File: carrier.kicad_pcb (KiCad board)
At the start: 4 copper layers, 20.3 x 68.6 mm, 41 parts, among them J1 Conn_02x06_Odd_Even, J10 Conn_01x02, J2 Conn_01x26, J3 Conn_01x26, J4 TYPE-C-31-M-12, J5 Conn_01x02, J6 Conn_01x02, J7 Conn_01x02, J8 Conn_01x02, J9 Conn_01x02, U1 CARAVEL, U2 W25Q128JVS, U3 LP5907MFX-3.3, U4 LP5907MFX-1.8, U5 LP5907MFX-1.8, U6 LP5907MFX-3.3, U7 TPD2E001DRSR, X1 SG-5032CAN

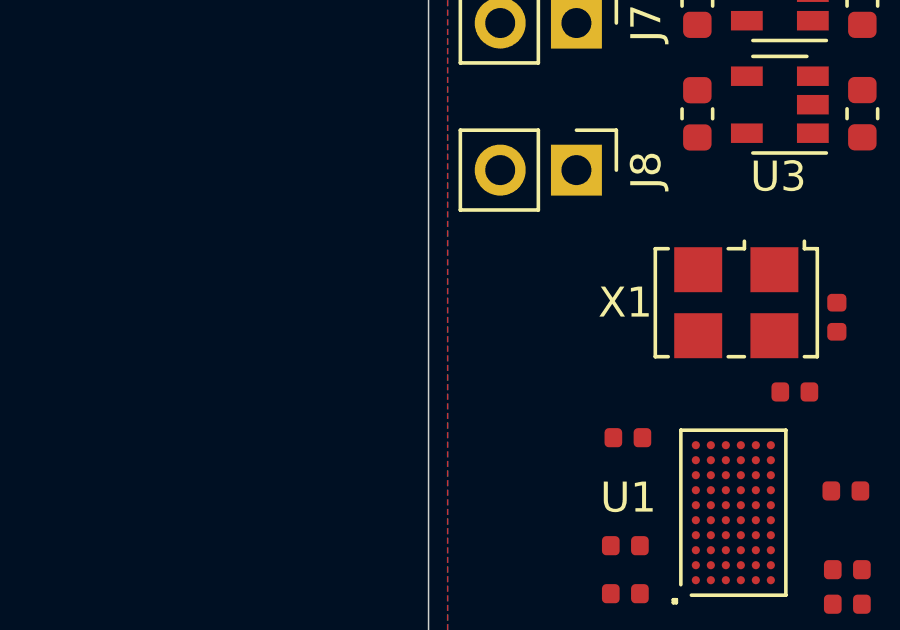
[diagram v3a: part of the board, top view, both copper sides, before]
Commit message: Add provision for external clk on  pin header
Uses a solder jumper to select oscillator by default.
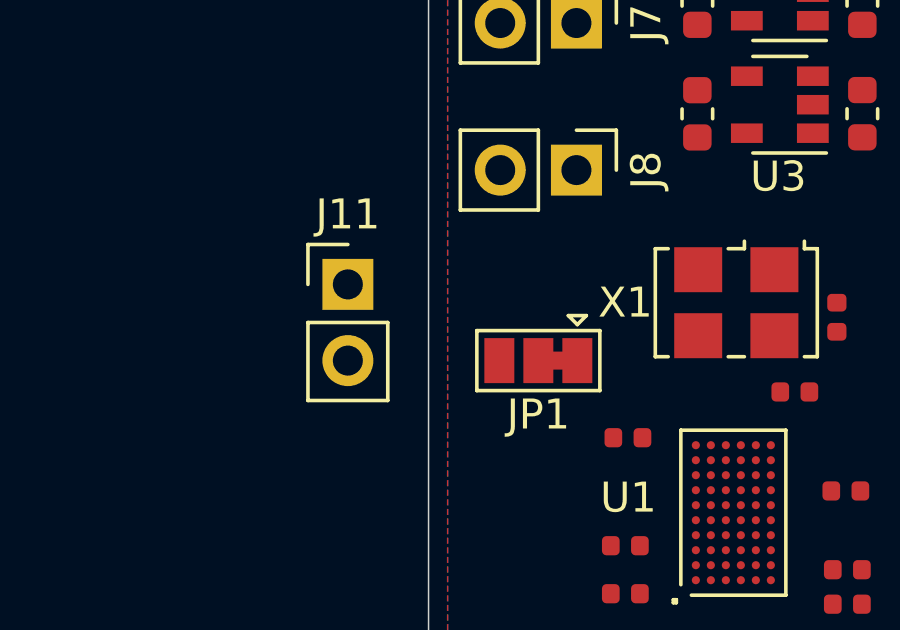
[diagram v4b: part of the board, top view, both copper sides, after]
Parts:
- added J11: Conn_01x02, Connector_PinHeader_2.54mm:PinHeader_1x02_P2.54mm_Vertical, F.Cu at (55.9, 72.4)
- added JP1: SolderJumper_3_Bridged12, Jumper:SolderJumper-3_P1.3mm_Bridged12_Pad1.0x1.5mm, F.Cu at (62.2, 74.9)
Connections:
- X1 pad 3: clock -> Net-(X1-Pad3)
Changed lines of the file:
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@@
   (net 78 "Net-(J4-PadA4B9)")
   (net 79 "unconnected-(J2-Pad3)")
+  (net 80 "Net-(X1-Pad3)")
+  (net 81 "Net-(J11-Pad1)")
   (footprint "Connector_PinHeader_2.54mm:PinHeader_1x26_P2.54mm_Vertical" (layer "F.Cu")
     (at 41.0972 46.6344)
@@
       (net 3 "GND") (pinfunction "GND") (pintype "power_in"))
     (pad "3" smd rect locked (at 1.27 -1.1 180) (size 1.6 1.5) (layers "F.Cu" "F.Paste" "F.Mask")
-      (net 22 "clock") (pinfunction "OUT") (pintype "output"))
+      (net 80 "Net-(X1-Pad3)") (pinfunction "OUT") (pintype "output"))
     (pad "4" smd rect locked (at -1.27 -1.1 180) (size 1.6 1.5) (layers "F.Cu" "F.Paste" "F.Mask")
       (net 7 "vdda") (pinfunction "VCC") (pintype "power_in"))
@@
     )
   )
+  (footprint "Jumper:SolderJumper-3_P1.3mm_Bridged12_Pad1.0x1.5mm" (layer "F.Cu")
+    (at 62.23 74.93 180)
+    (descr "SMD Solder 3-pad Jumper, 1x1.5mm Pads, 0.3mm gap, pads 1-2 bridged with 1 copper strip")
+    (tags "solder jumper open")
+    (property "Sheetfile" "carrier.kicad_sch")
+    (property "Sheetname" "")
+    (attr exclude_from_pos_files)
+    (fp_text reference "JP1" (at 0 -1.8) (layer "F.SilkS")
+      (effects (font (size 1 1) (thickness 0.15)))
+    )
+    (fp_text value "SolderJumper_3_Bridged12" (at 0 2) (layer "F.Fab")
+      (effects (font (size 1 1) (thickness 0.15)))
+    )
+    (fp_poly (pts
+        (xy -0.9 -0.3)
+        (xy -0.4 -0.3)
+        (xy -0.4 0.3)
+        (xy -0.9 0.3)
+      ) (layer "F.Cu") (width 0) (fill solid))
+    (fp_line (start 2.05 -1) (end 2.05 1) (layer "F.SilkS") (width 0.12))
+    (fp_line (start -1.3 1.2) (end -1 1.5) (layer "F.SilkS") (width 0.12))
+    (fp_line (start 2.05 1) (end -2.05 1) (layer "F.SilkS") (width 0.12))
+    (fp_line (start -2.05 1) (end -2.05 -1) (layer "F.SilkS") (width 0.12))
+    (fp_line (start -1.6 1.5) (end -1 1.5) (layer "F.SilkS") (width 0.12))
+    (fp_line (start -1.3 1.2) (end -1.6 1.5) (layer "F.SilkS") (width 0.12))
+    (fp_line (start -2.05 -1) (end 2.05 -1) (layer "F.SilkS") (width 0.12))
+    (fp_line (start 2.3 1.25) (end -2.3 1.25) (layer "F.CrtYd") (width 0.05))
+    (fp_line (start -2.3 -1.25) (end 2.3 -1.25) (layer "F.CrtYd") (width 0.05))
+    (fp_line (start 2.3 1.25) (end 2.3 -1.25) (layer "F.CrtYd") (width 0.05))
+    (fp_line (start -2.3 -1.25) (end -2.3 1.25) (layer "F.CrtYd") (width 0.05))
+    (pad "1" smd rect locked (at -1.3 0 180) (size 1 1.5) (layers "F.Cu" "F.Mask")
+      (net 80 "Net-(X1-Pad3)") (pinfunction "A") (pintype "passive"))
+    (pad "2" smd rect locked (at 0 0 180) (size 1 1.5) (layers "F.Cu" "F.Mask")
+      (net 22 "clock") (pinfunction "C") (pintype "input"))
+    (pad "3" smd rect locked (at 1.3 0 180) (size 1 1.5) (layers "F.Cu" "F.Mask")
+      (net 81 "Net-(J11-Pad1)") (pinfunction "B") (pintype "passive"))
+  )
   (footprint "TPD2E001DRSR:SON95P315X315X80-7N" (layer "F.Cu")
     (at 113.4618 72.4408 -90)
@@
       (effects (font (size 1.642031 1.642031) (thickness 0.015)))
     )
+    (fp_line (start -0.3048 -1.5748) (end -1.5748 -1.5748) (layer "F.SilkS") (width 0.1524))
     (fp_line (start 0.3048 -1.5748) (end -0.3048 -1.5748) (layer "F.SilkS") (width 0.1524))
-    (fp_line (start -0.3048 -1.5748) (end -1.5748 -1.5748) (layer "F.SilkS") (width 0.1524))
+    (fp_line (start 1.5748 -1.5748) (end 0.3048 -1.5748) (layer "F.SilkS") (width 0.1524))
     (fp_line (start -1.5748 1.5748) (end 1.5748 1.5748) (layer "F.SilkS") (width 0.1524))
-    (fp_line (start 1.5748 -1.5748) (end 0.3048 -1.5748) (layer "F.SilkS") (width 0.1524))
     (fp_arc (start 0.019089 -1.577994) (end -0.3048 -1.5748) (angle -52) (layer "F.SilkS") (width 0.1524))
     (fp_arc (start -0.019089 -1.577994) (end 0.1778 -1.3208) (angle -52) (layer "F.SilkS") (width 0.1524))
     (fp_line (start -0.3048 -1.5748) (end -1.5748 -1.5748) (layer "F.Fab") (width 0.1))
+    (fp_line (start 1.5748 1.5748) (end 1.5748 -1.5748) (layer "F.Fab") (width 0.1))
     (fp_line (start -1.5748 -1.5748) (end -1.5748 1.5748) (layer "F.Fab") (width 0.1))
     (fp_line (start -1.5748 1.5748) (end 1.5748 1.5748) (layer "F.Fab") (width 0.1))
+    (fp_line (start 0.3048 -1.5748) (end -0.3048 -1.5748) (layer "F.Fab") (width 0.1))
     (fp_line (start 1.5748 -1.5748) (end 0.3048 -1.5748) (layer "F.Fab") (width 0.1))
-    (fp_line (start 1.5748 1.5748) (end 1.5748 -1.5748) (layer "F.Fab") (width 0.1))
-    (fp_line (start 0.3048 -1.5748) (end -0.3048 -1.5748) (layer "F.Fab") (width 0.1))
     (fp_arc (start 0 -1.5748) (end -0.3048 -1.5748) (angle -180) (layer "F.Fab") (width 0.1))
     (pad "1" smd rect locked (at -1.4478 -0.9398 270) (size 0.8636 0.4064) (layers "F.Cu" "F.Paste" "F.Mask")
@@
     )
   )
+  (footprint "Connector_PinHeader_2.54mm:PinHeader_1x02_P2.54mm_Vertical" (layer "F.Cu")
+    (at 55.88 72.39)
+    (descr "Through hole straight pin header, 1x02, 2.54mm pitch, single row")
+    (tags "Through hole pin header THT 1x02 2.54mm single row")
+    (property "Sheetfile" "carrier.kicad_sch")
+    (property "Sheetname" "")
+    (attr through_hole)
+    (fp_text reference "J11" (at 0 -2.33) (layer "F.SilkS")
+      (effects (font (size 1 1) (thickness 0.15)))
+    )
+    (fp_text value "Conn_01x02" (at 0 4.87) (layer "F.Fab")
+      (effects (font (size 1 1) (thickness 0.15)))
+    )
+    (fp_text user "${REFERENCE}" (at 0 1.27 90) (layer "F.Fab")
+      (effects (font (size 1 1) (thickness 0.15)))
+    )
+    (fp_line (start 1.33 1.27) (end 1.33 3.87) (layer "F.SilkS") (width 0.12))
+    (fp_line (start -1.33 -1.33) (end 0 -1.33) (layer "F.SilkS") (width 0.12))
+    (fp_line (start -1.33 3.87) (end 1.33 3.87) (layer "F.SilkS") (width 0.12))
+    (fp_line (start -1.33 1.27) (end -1.33 3.87) (layer "F.SilkS") (width 0.12))
+    (fp_line (start -1.33 0) (end -1.33 -1.33) (layer "F.SilkS") (width 0.12))
+    (fp_line (start -1.33 1.27) (end 1.33 1.27) (layer "F.SilkS") (width 0.12))
+    (fp_line (start -1.8 -1.8) (end -1.8 4.35) (layer "F.CrtYd") (width 0.05))
+    (fp_line (start 1.8 -1.8) (end -1.8 -1.8) (layer "F.CrtYd") (width 0.05))
+    (fp_line (start -1.8 4.35) (end 1.8 4.35) (layer "F.CrtYd") (width 0.05))
+    (fp_line (start 1.8 4.35) (end 1.8 -1.8) (layer "F.CrtYd") (width 0.05))
+    (fp_line (start -1.27 3.81) (end -1.27 -0.635) (layer "F.Fab") (width 0.1))
+    (fp_line (start -0.635 -1.27) (end 1.27 -1.27) (layer "F.Fab") (width 0.1))
+    (fp_line (start 1.27 -1.27) (end 1.27 3.81) (layer "F.Fab") (width 0.1))
+    (fp_line (start -1.27 -0.635) (end -0.635 -1.27) (layer "F.Fab") (width 0.1))
+    (fp_line (start 1.27 3.81) (end -1.27 3.81) (layer "F.Fab") (width 0.1))
+    (pad "1" thru_hole rect locked (at 0 0) (size 1.7 1.7) (drill 1) (layers *.Cu *.Mask)
+      (net 81 "Net-(J11-Pad1)") (pinfunction "Pin_1") (pintype "passive"))
+    (pad "2" thru_hole oval locked (at 0 2.54) (size 1.7 1.7) (drill 1) (layers *.Cu *.Mask)
+      (net 3 "GND") (pinfunction "Pin_2") (pintype "passive"))
+    (model "${KISYS3DMOD}/Connector_PinHeader_2.54mm.3dshapes/PinHeader_1x02_P2.54mm_Vertical.wrl"
+      (offset (xyz 0 0 0))
+      (scale (xyz 1 1 1))
+      (rotate (xyz 0 0 0))
+    )
+  )
   (footprint "Capacitor_SMD:C_0402_1005Metric" (layer "F.Cu")
     (at 114.2238 77.089 -90)
@@
       (effects (font (size 1 1) (thickness 0.15)))
     )
+    (fp_line (start -4.47 2.6) (end -4.47 1.37) (layer "F.SilkS") (width 0.127))
+    (fp_line (start 4.47 -2.81) (end 4.47 -1.37) (layer "F.SilkS") (width 0.127))
+    (fp_line (start -4.47 -2.81) (end -4.47 -1.37) (layer "F.SilkS") (width 0.127))
     (fp_line (start 4.47 1.37) (end 4.47 2.6) (layer "F.SilkS") (width 0.127))
     (fp_line (start 4.47 2.6) (end -4.47 2.6) (layer "F.SilkS") (width 0.127))
-    (fp_line (start -4.47 -2.81) (end -4.47 -1.37) (layer "F.SilkS") (width 0.127))
-    (fp_line (start 4.47 -2.81) (end 4.47 -1.37) (layer "F.SilkS") (width 0.127))
-    (fp_line (start -4.47 2.6) (end -4.47 1.37) (layer "F.SilkS") (width 0.127))
     (fp_circle (center -3.4 -6.4) (end -3.3 -6.4) (layer "F.SilkS") (width 0.2) (fill none))
+    (fp_line (start 5.095 2.85) (end 5.095 -6.07) (layer "F.CrtYd") (width 0.05))
+    (fp_line (start -5.095 -6.07) (end -5.095 2.85) (layer "F.CrtYd") (width 0.05))
+    (fp_line (start -5.095 2.85) (end 5.095 2.85) (layer "F.CrtYd") (width 0.05))
     (fp_line (start 5.095 -6.07) (end -5.095 -6.07) (layer "F.CrtYd") (width 0.05))
-    (fp_line (start -5.095 -6.07) (end -5.095 2.85) (layer "F.CrtYd") (width 0.05))
-    (fp_line (start 5.095 2.85) (end 5.095 -6.07) (layer "F.CrtYd") (width 0.05))
-    (fp_line (start -5.095 2.85) (end 5.095 2.85) (layer "F.CrtYd") (width 0.05))
     (fp_line (start -4.47 -4.7) (end -4.47 2.6) (layer "F.Fab") (width 0.127))
     (fp_line (start 4.47 -4.7) (end -4.47 -4.7) (layer "F.Fab") (width 0.127))

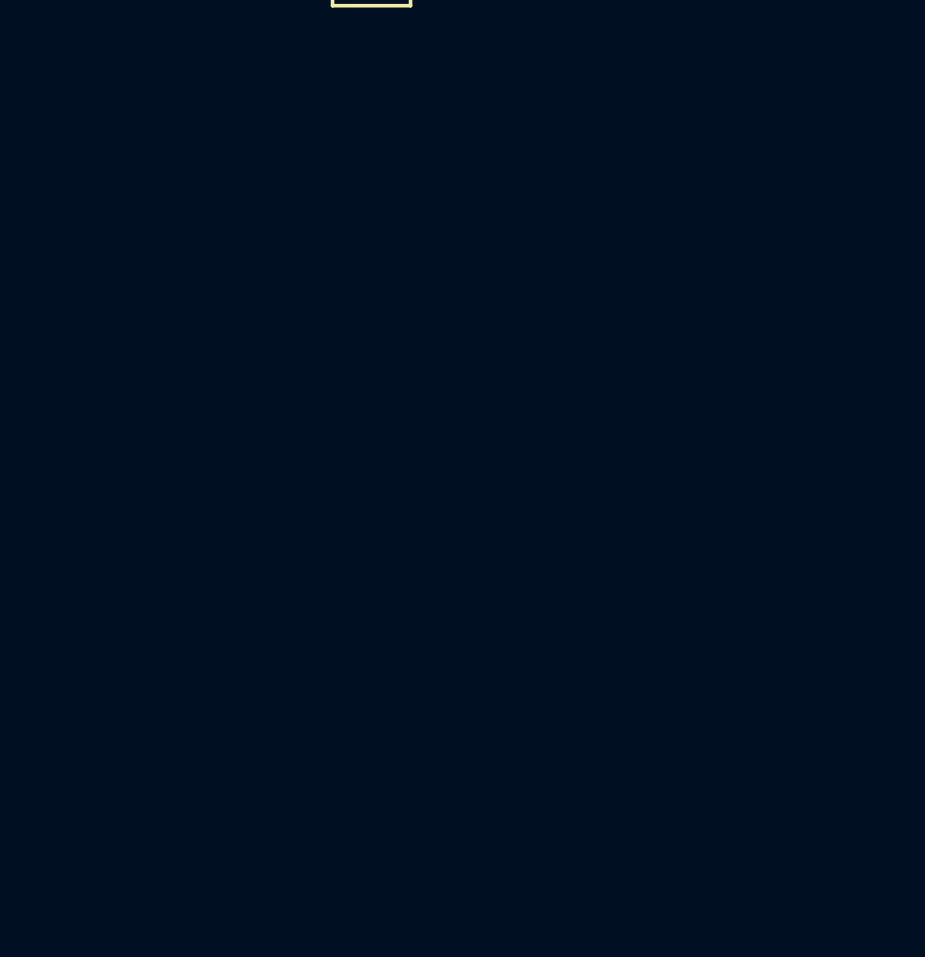
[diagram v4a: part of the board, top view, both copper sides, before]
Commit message: Add audio circuitry
Adds headphone output for the PCM audio output
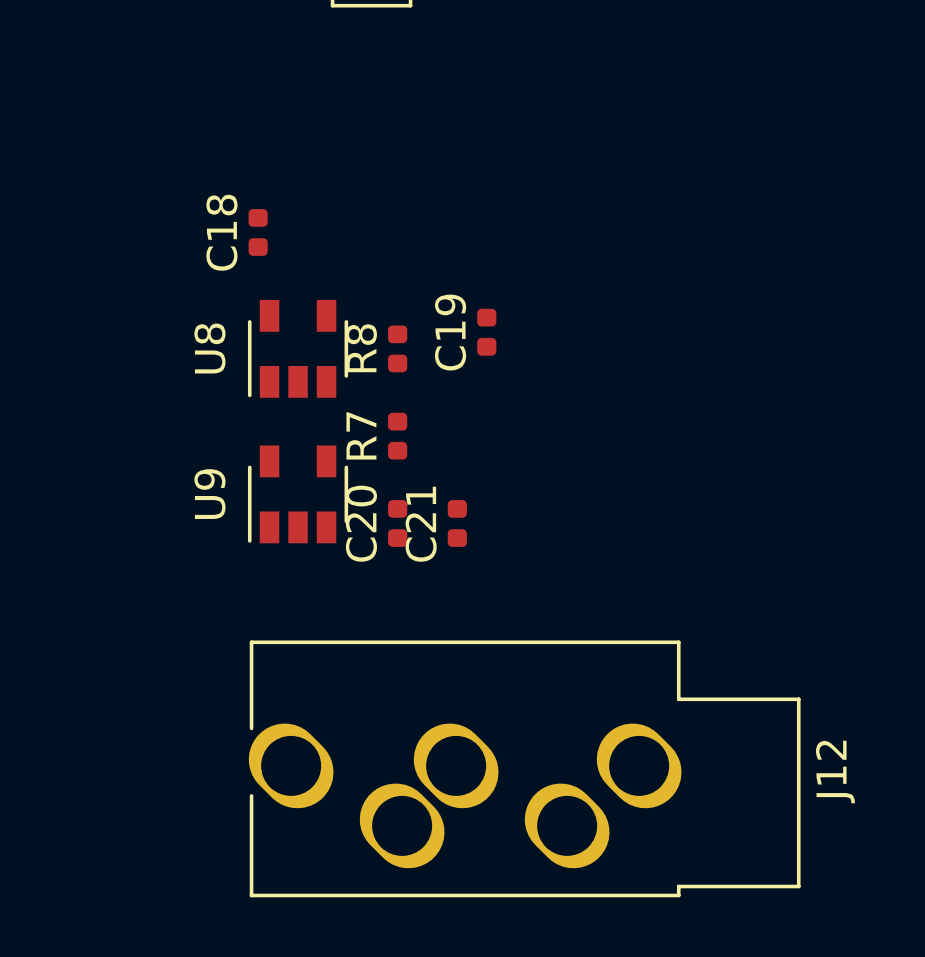
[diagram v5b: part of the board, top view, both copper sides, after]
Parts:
- added C18: 100n, Capacitor_SMD:C_0402_1005Metric, F.Cu at (113.0, 90.2)
- added C19: 100n, Capacitor_SMD:C_0402_1005Metric, F.Cu at (120.7, 93.5)
- added C20: 100n, Capacitor_SMD:C_0402_1005Metric, F.Cu at (117.7, 99.9)
- added C21: 100n, Capacitor_SMD:C_0402_1005Metric, F.Cu at (119.7, 99.9)
- added J12: AudioJack3_SwitchTR, Connector_Audio:Jack_3.5mm_CUI_SJ1-3535NG_Horizontal_CircularHoles, F.Cu at (125.7, 108.0)
- added R7: 100 Ohm, Resistor_SMD:R_0402_1005Metric, F.Cu at (117.7, 97.0)
- added R8: 100 Ohm, Resistor_SMD:R_0402_1005Metric, F.Cu at (117.7, 94.0)
- added U8: OPA340NA, Package_TO_SOT_SMD:SOT-23-5, F.Cu at (114.4, 94.0)
- added U9: OPA340NA, Package_TO_SOT_SMD:SOT-23-5, F.Cu at (114.4, 98.9)
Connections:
- U1 pad D1: mprj_io[18] -> pcm_audio_2
- U1 pad D2: mprj_io[17] -> pcm_audio_1
